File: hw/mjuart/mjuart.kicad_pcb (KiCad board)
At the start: 4 copper layers, 24.5 x 14 mm, 16 parts, among them J1 S4B-ZR-SM4A-TFLFSN, J2 USB4110-GF-A, J3 Conn_01x04_Pin, J4 Conn_01x04_Pin, U1 FT231XQ

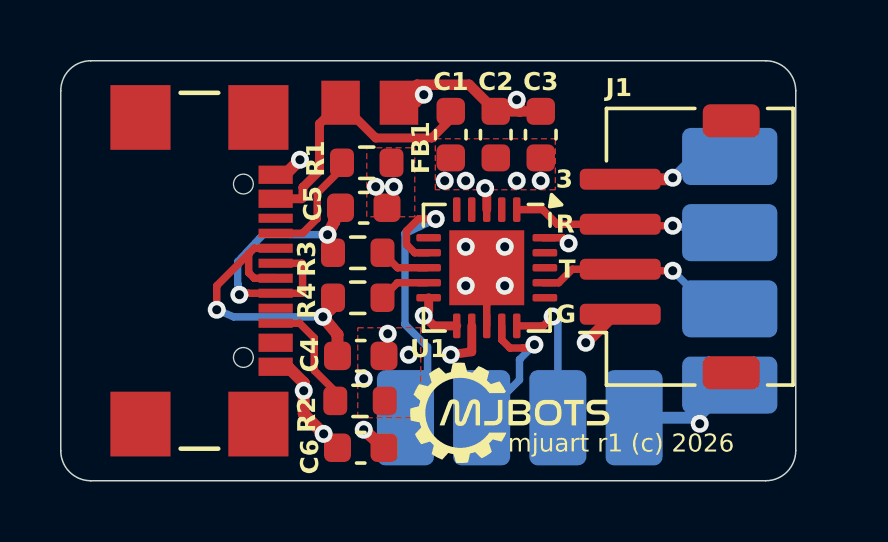
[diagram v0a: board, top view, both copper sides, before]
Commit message: mjuart: Fill in all BOM entries and slight layout tweaks
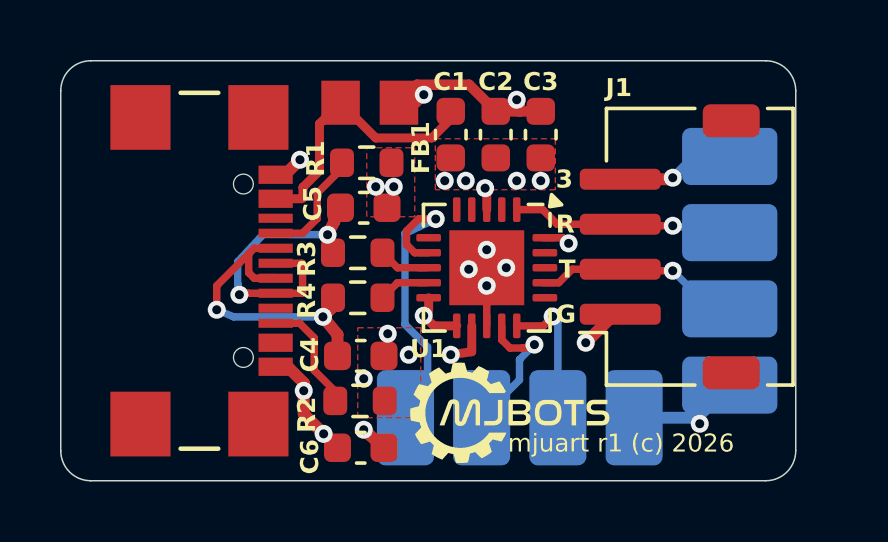
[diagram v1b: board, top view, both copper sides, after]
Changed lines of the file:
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@@
 	)
 	(via
-		(at 153.5 106.2)
+		(at 154.2 106.3)
 		(size 0.6)
 		(drill 0.3)
@@
 	)
 	(via
-		(at 154.8 107.5)
+		(at 154.2 107.5)
 		(size 0.6)
 		(drill 0.3)
@@
 	)
 	(via
-		(at 153.5 107.5)
+		(at 153.6 106.95)
 		(size 0.6)
 		(drill 0.3)
@@
 	)
 	(via
-		(at 154.8 106.2)
+		(at 154.85 106.9)
 		(size 0.6)
 		(drill 0.3)

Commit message: mjuart: Fix all ERC and DRC violations
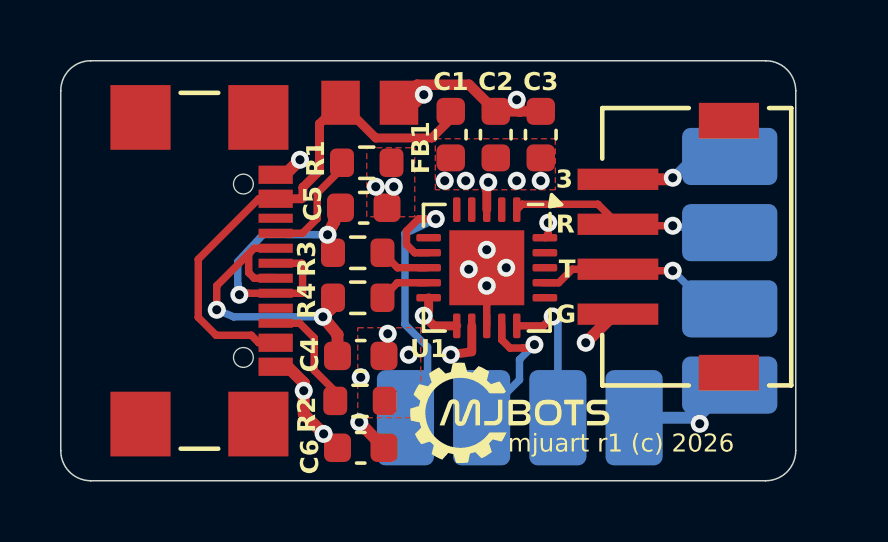
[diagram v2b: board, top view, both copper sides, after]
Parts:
- C4, C5: value 47pF -> 22pF
- J1: footprint Connector_JST:JST_ZH_S4B-ZR-SM4A-TF_1x04-1MP_P1.50mm_Horizontal -> footprints:CONN_S4B-ZR-SM4A-TF_JST
- moved J1 0.90 mm to (161.2, 106.2), turned to -90 degrees
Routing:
- net Net-(C1-Pad1): track 9.28 -> 17.6 mm
